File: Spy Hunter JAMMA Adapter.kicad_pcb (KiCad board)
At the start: 2 copper layers, 111.4 x 135.4 mm, 88 parts, among them P1 1K, P2 1K, P3 10K, P4 1K, SW2 SW_DIP_SPSTx02_Slide_9.78x7.2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, U1 74LS86, U10 NE555, U11 LM386, U12 CD4099B, U2 74LS74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

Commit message: correct RVR/RV12 effects labels, swap music pot around
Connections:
- MCRJ3 pad 1: EFFECTS_RVR -> EFFECTS_RV12
- MCRJ3 pad 3: EFFECTS_RV12 -> EFFECTS_RVR
- P1 pad 1: EFFECTS_RV12 -> EFFECTS_RVR
- P1 pad 3: EFFECTS_RVR -> EFFECTS_RV12
- P2 pad 1: MUSIC_RV12 -> MUSIC_RVR
- P2 pad 3: MUSIC_RVR -> MUSIC_RV12
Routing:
- net MUSIC_RV12: track 115.2 -> 109.7 mm
- net MUSIC_RVR: track 106.9 -> 111.9 mm
- net EFFECTS_RVR: track 56.6 -> 60.5 mm
- net EFFECTS_RV12: track 60.5 -> 56.6 mm
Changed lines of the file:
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@@
 	(net 5 "VIDEO_G")
 	(net 6 "+12V")
-	(net 7 "EFFECTS_RVR")
+	(net 7 "EFFECTS_RV12")
 	(net 8 "EFFECTS_RVS")
-	(net 9 "EFFECTS_RV12")
+	(net 9 "EFFECTS_RVR")
 	(net 10 "AUDIO_OUT")
 	(net 11 "1P_D")
@@
 			(layers "*.Cu" "*.Mask")
 			(remove_unused_layers no)
-			(net 9 "EFFECTS_RV12")
+			(net 9 "EFFECTS_RVR")
 		)
 		(pad "2" thru_hole circle
@@
 			(layers "*.Cu" "*.Mask")
 			(remove_unused_layers no)
-			(net 7 "EFFECTS_RVR")
+			(net 7 "EFFECTS_RV12")
 		)
 		(embedded_fonts no)
@@
 			(layers "*.Cu" "*.Mask")
 			(remove_unused_layers no)
-			(net 7 "EFFECTS_RVR")
+			(net 7 "EFFECTS_RV12")
 		)
 		(pad "2" thru_hole circle
@@
 			(layers "*.Cu" "*.Mask")
 			(remove_unused_layers no)
-			(net 9 "EFFECTS_RV12")
+			(net 9 "EFFECTS_RVR")
 		)
 		(pad "4" thru_hole circle
@@
 			(layers "*.Cu" "*.Mask")
 			(remove_unused_layers no)
-			(net 81 "MUSIC_RV12")
+			(net 79 "MUSIC_RVR")
 		)
 		(pad "2" thru_hole circle
@@
 			(layers "*.Cu" "*.Mask")
 			(remove_unused_layers no)
-			(net 79 "MUSIC_RVR")
+			(net 81 "MUSIC_RV12")
 		)
 		(embedded_fonts no)
@@
 		)
 	)
-	(gr_text "RVR"
+	(gr_text "RV12"
 		(at 63.91675 67.582987 0)
 		(layer "F.SilkS")
@@
 		)
 	)
-	(gr_text "RV12"
+	(gr_text "RVR"
 		(at 63.91675 72.86 0)
 		(layer "F.SilkS")
@@
 	)
 	(segment
-		(start 115.095 53.4)
-		(end 112.315 56.18)
+		(start 110.095 53.4)
+		(end 107.315 56.18)
 		(width 0.4)
 		(layer "B.Cu")
@@
 	)
 	(segment
-		(start 153.365 103.865)
-		(end 151.765 102.265)
+		(start 122.4 53.4)
+		(end 110.095 53.4)
 		(width 0.4)
 		(layer "B.Cu")
@@
 	)
 	(segment
-		(start 133.725051 51.865)
-		(end 148.926645 67.066595)
+		(start 153.365 103.865)
+		(end 151.765 102.265)
 		(width 0.4)
 		(layer "B.Cu")
@@
 	)
 	(segment
-		(start 122.4 53.4)
-		(end 115.095 53.4)
+		(start 133.725051 51.865)
+		(end 148.926645 67.066595)
 		(width 0.4)
 		(layer "B.Cu")
@@
 	)
 	(segment
+		(start 121.012765 57.261)
+		(end 114.4 57.261)
+		(width 0.4)
+		(layer "B.Cu")
+		(net 81)
+	)
+	(segment
 		(start 148.165 67.012056)
 		(end 148.165 86.700694)
@@
 	)
 	(segment
-		(start 121.012765 57.261)
-		(end 108.396 57.261)
+		(start 114.4 57.261)
+		(end 113.396 57.261)
 		(width 0.4)
 		(layer "B.Cu")
@@
 	)
 	(segment
-		(start 108.396 57.261)
-		(end 107.315 56.18)
-		(width 0.4)
-		(layer "B.Cu")
-		(net 81)
-	)
-	(segment
 		(start 152.865 117.916785)
 		(end 152.865 104.425661)
@@
 		(width 0.4)
 		(layer "B.Cu")
+		(net 81)
+	)
+	(segment
+		(start 113.396 57.261)
+		(end 112.66926 56.53426)
+		(width 0.4)
+		(layer "B.Cu")

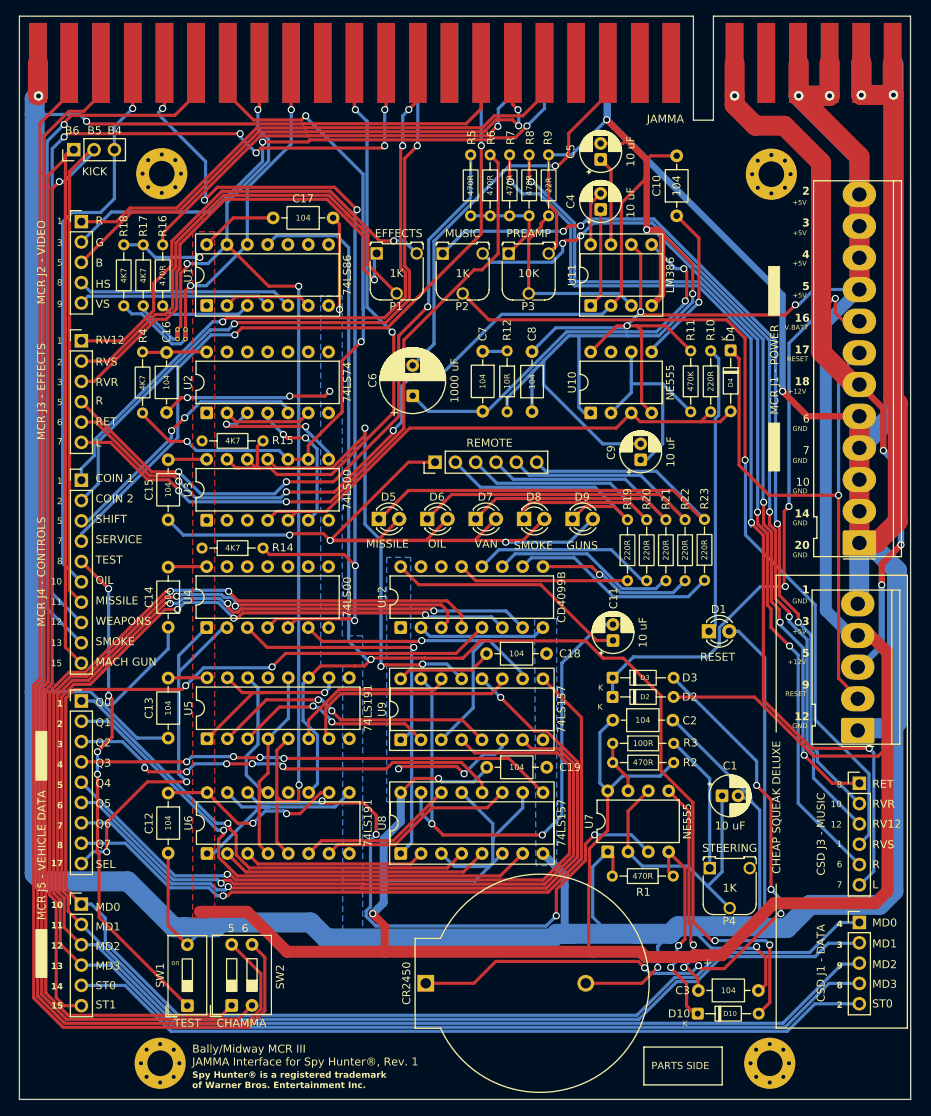
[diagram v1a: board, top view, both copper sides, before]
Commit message: slightly widen boards
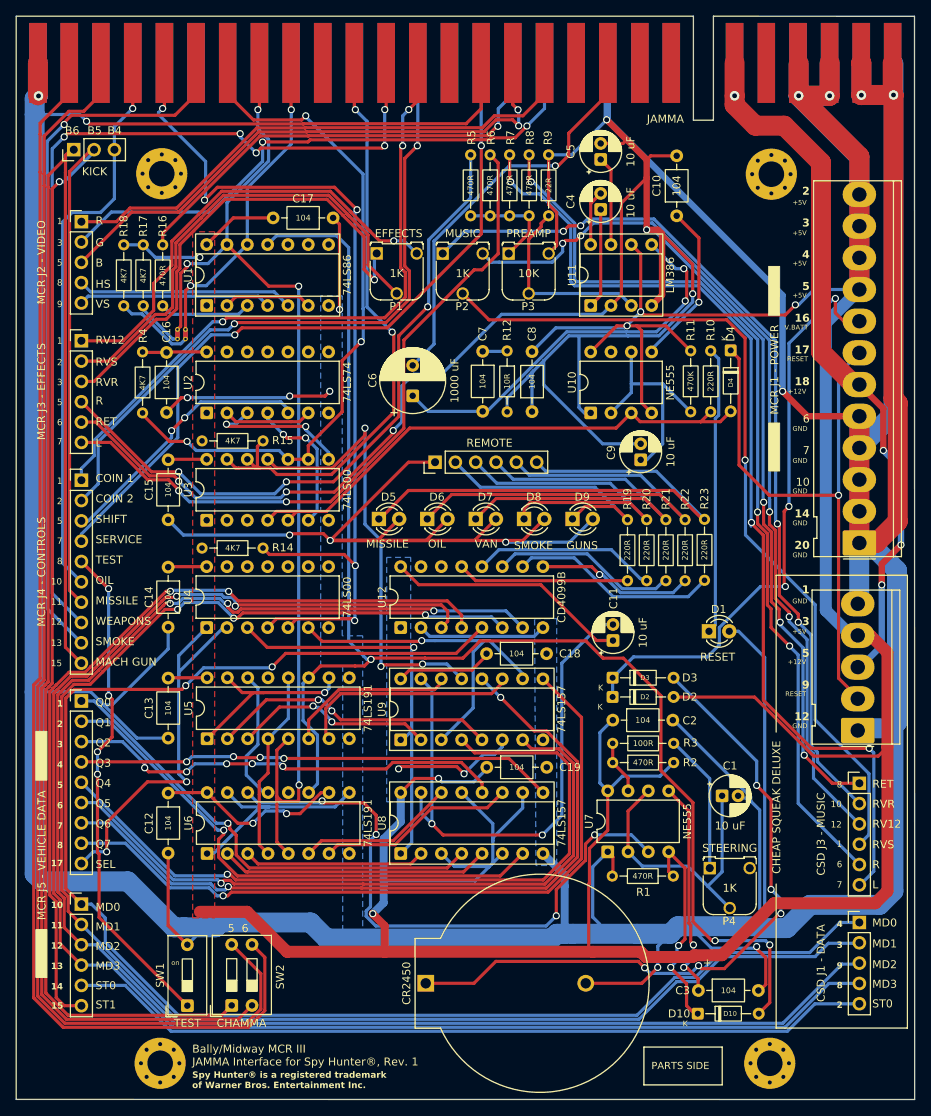
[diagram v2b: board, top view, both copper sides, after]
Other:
- board size 111.4 x 135.4 mm -> 112.3 x 135.4 mm
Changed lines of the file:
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@@
 	(gr_poly
 		(pts
-			(xy 138.655 39.515005) (xy 141.155 39.515005) (xy 141.155 26.515) (xy 165.795728 26.515144) (xy 165.814722 161.917773)
-			(xy 54.405001 161.915663) (xy 54.404997 26.515) (xy 138.655 26.515)
+			(xy 138.655 39.515005) (xy 141.155 39.515005) (xy 141.155 26.515) (xy 166.29266 26.524129) (xy 166.311654 161.926767)
+			(xy 54.005001 161.915656) (xy 54.004997 26.515) (xy 138.655 26.515)
 		)
 		(stroke
